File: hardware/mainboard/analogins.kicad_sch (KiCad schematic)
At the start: 27 parts, among them J3 CASTOR PITCH, J4 POLLUX PITCH, J5 CASTOR DUTY, J6 POLLUX DUTY, U6 MCP6004

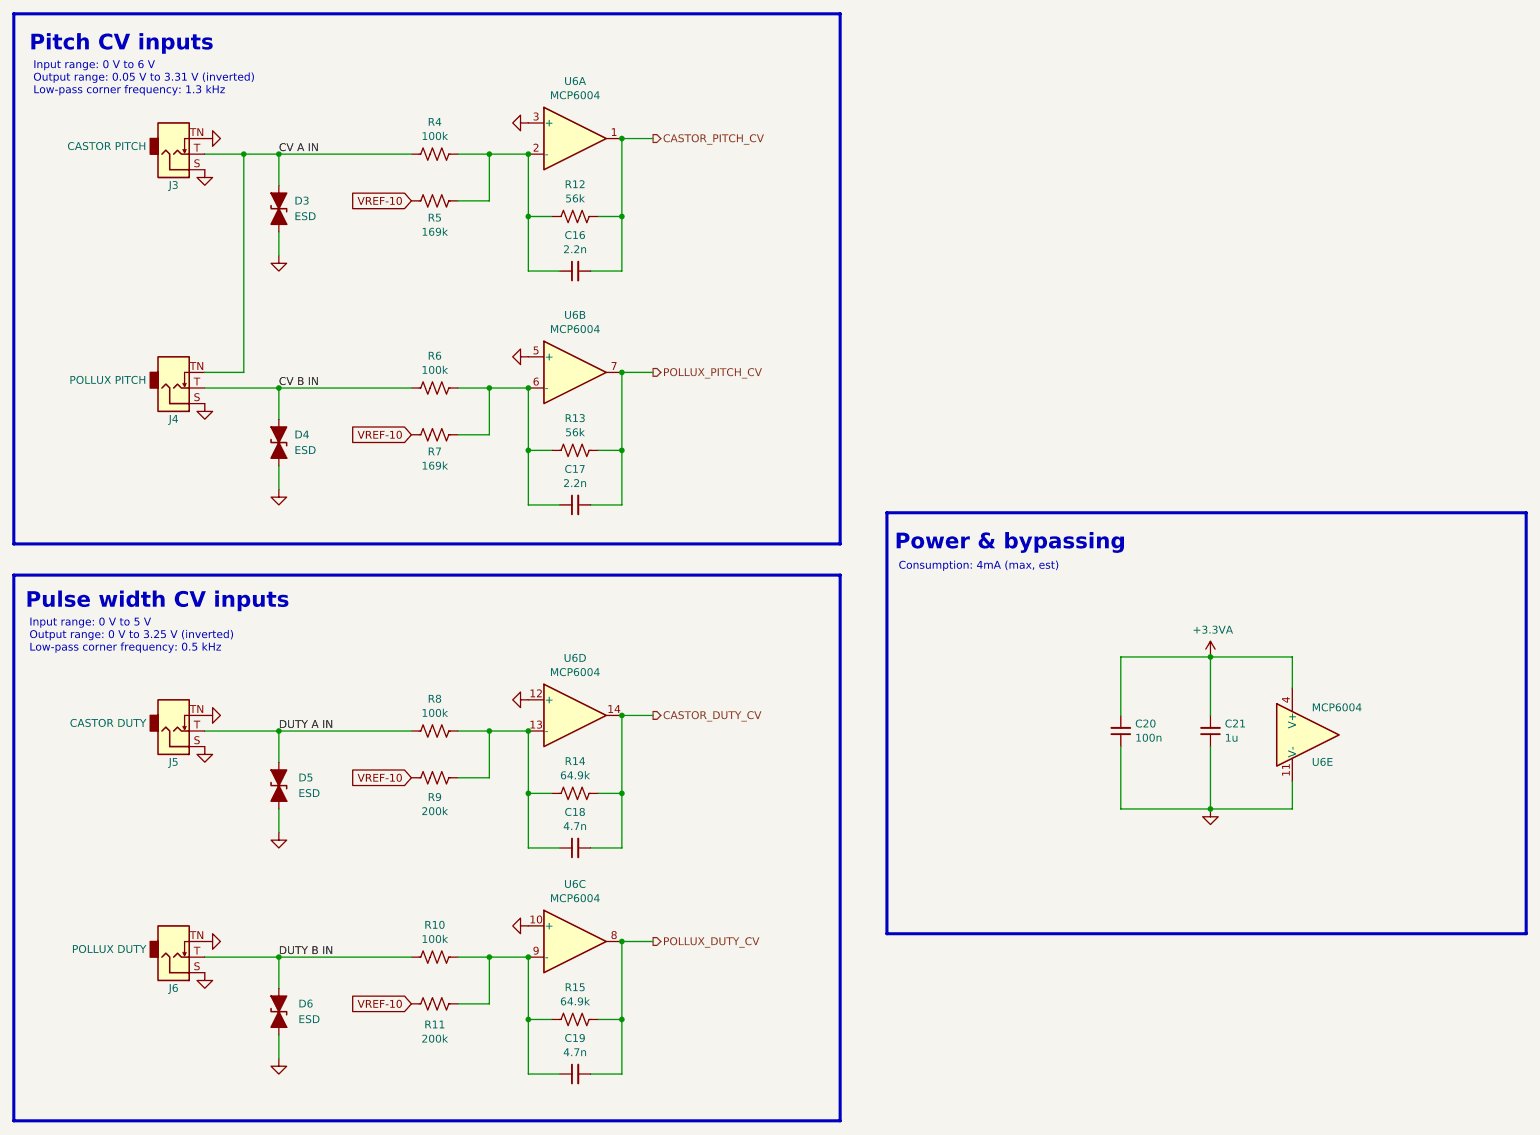
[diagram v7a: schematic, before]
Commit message: Audit BOM, replace some parts with alts
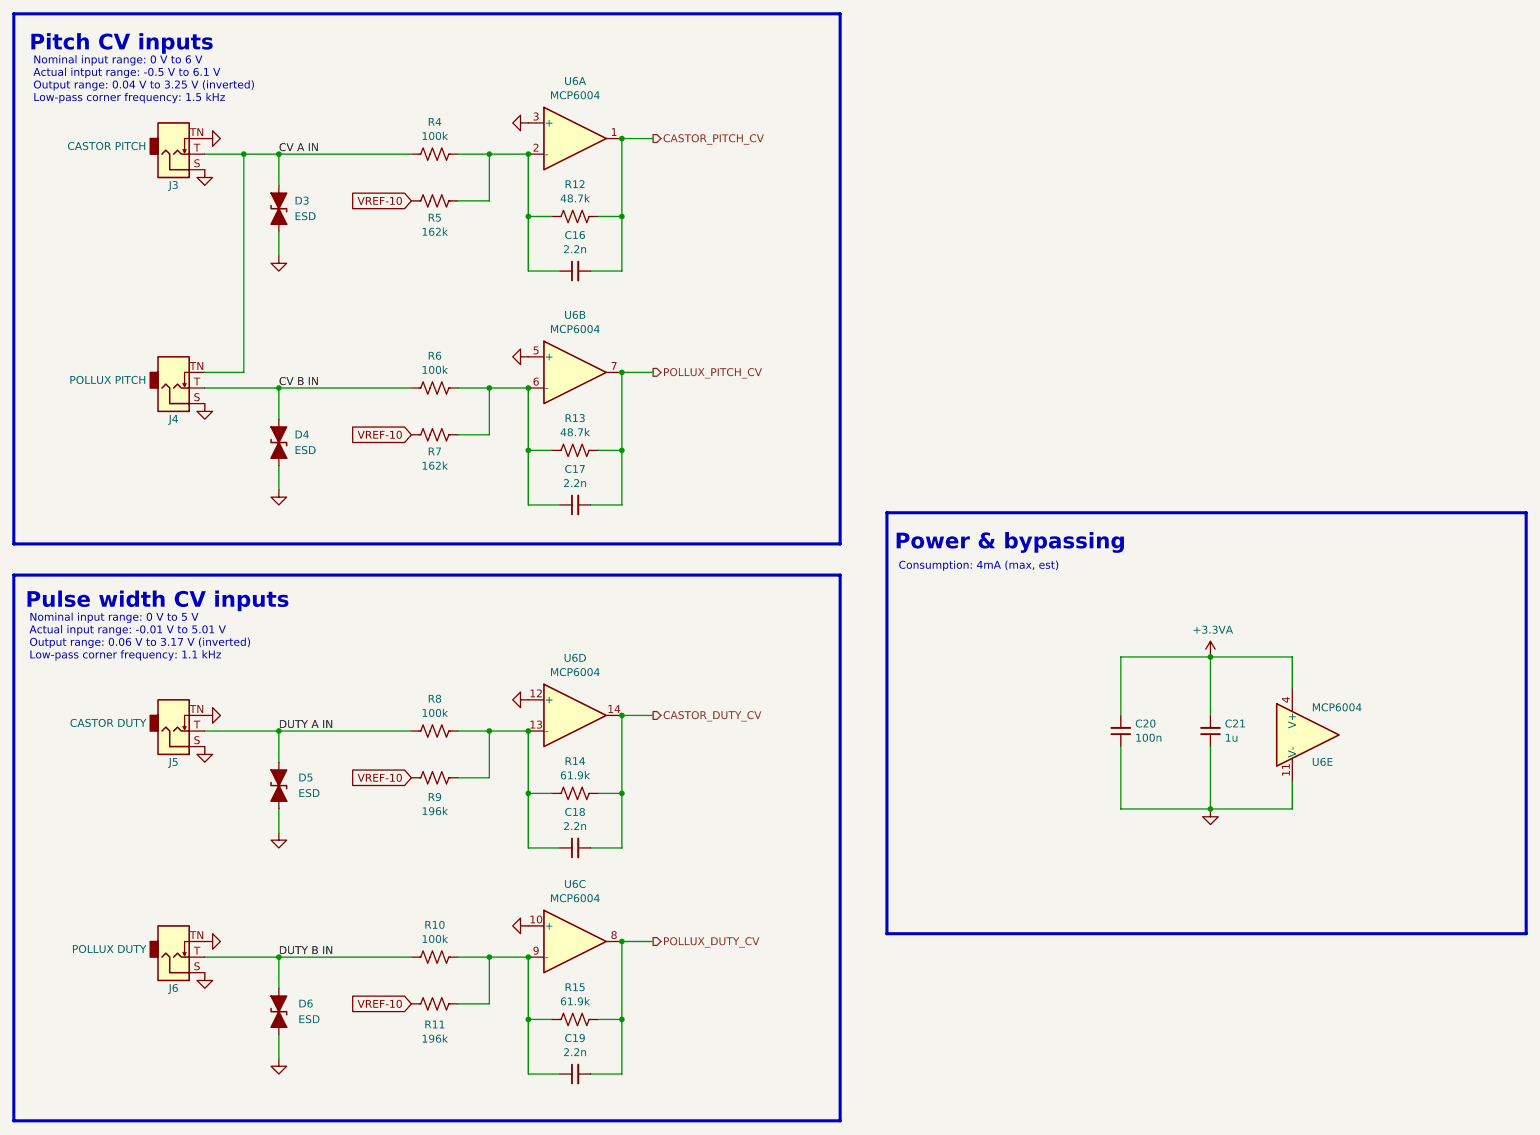
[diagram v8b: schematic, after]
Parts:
- C16, C17: finalized (none) -> yes; mpn (none) -> GRM155R71H222KA01D
- C18, C19: value 4.7n -> 2.2n; finalized (none) -> yes; mpn (none) -> GRM155R71H222KA01D
- C20: finalized (none) -> yes; macrofab_mpn (none) -> MF-CAP-0402-0.1uF; mpn (none) -> CL05B104KO5NNNC
- C21: finalized (none) -> yes; macrofab_mpn (none) -> MF-CAP-0402-1uF; mpn (none) -> CL05A105KO5NNNC
- D3, D4, D5, D6, U6: finalized (none) -> yes
- R10, R4, R6, R8: Reqs Analog input, 0.5%, 2 mW -> Analog input, 0.5%, 100 mW, thin film
- R11, R9: value 200k -> 196k; Reqs Analog input, 0.5%, 1 mW -> Analog input, 0.5%, 100 mW, thin film
- R12, R13: value 56k -> 48.7k; Reqs Analog input, 0.5%, 3 mW -> Analog input, 0.5%, 100 mW, thin film
- R14, R15: value 64.9k -> 61.9k; Reqs Analog input, 1%, 3 mW -> Analog input, 1%, 100 mW, thin film
- R5, R7: value 169k -> 162k; Reqs Analog input, 0.5%, 1 mW -> Analog input, 0.5%, 100 mW, thin film
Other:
- note added: "Nominal input range: 0 V to 5 V Actual input range: -0.01 V to 5.01 V Output range: 0.06 V to 3.17 V (inverted) Low-pass corner frequency: 1.1 kHz"
- note added: "Nominal input range: 0 V to 6 V Actual intput range: -0.5 V to 6.1 V Output range: 0.04 V to 3.25 V (inverted) Low-pass corner frequency: 1.5 kHz"
- note removed: "Input range: 0 V to 5 V Output range: 0 V to 3.25 V (inverted) Low-pass corner frequency: 0.5 kHz"
- note removed: "Input range: 0 V to 6 V Output range: 0.05 V to 3.31 V (inverted) Low-pass corner frequency: 1.3 kHz"
